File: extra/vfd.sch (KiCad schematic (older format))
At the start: 42 parts, among them P10 GU128x64E-U100, P11 gui140x16j-7002, P12 digital_in, P13 digital_out, U3 74LS125, U4 74LS125, U5 74LS125, U6 74LS125, U7 74LS125, U8 74LS245

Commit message: 3.3v is no longer connected to 5v!
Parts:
- removed R40: R?, xnorman:Resistor_Horizontal_RM10mm-xnorman, symbol R
- removed U8: 74LS245, Housings_DIP:DIP-20_W7.62mm_LongPads, symbol 74LS245
- added U8: 74LS245-xnor, Housings_DIP:DIP-20_W7.62mm_LongPads, symbol 74LS245-xnor
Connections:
- wire segments 279 -> 278
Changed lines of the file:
@@
 5v
 $Comp
-L GND #PWR018
+L GND #PWR019
 U 1 1 58578899
 P 750 650
-F 0 "#PWR018" H 750 400 50  0001 C CNN
+F 0 "#PWR019" H 750 400 50  0001 C CNN
 F 1 "GND" H 750 500 50  0000 C CNN
 F 2 "" H 750 650 50  0000 C CNN
@@
 vfdD7
 $Comp
-L GND #PWR019
+L GND #PWR020
 U 1 1 5857965E
 P 1350 7050
-F 0 "#PWR019" H 1350 6800 50  0001 C CNN
+F 0 "#PWR020" H 1350 6800 50  0001 C CNN
 F 1 "GND" H 1350 6900 50  0000 C CNN
 F 2 "" H 1350 7050 50  0000 C CNN
@@
 $EndComp
 $Comp
-L GND #PWR020
+L GND #PWR021
 U 1 1 585796B9
 P 1350 6450
-F 0 "#PWR020" H 1350 6200 50  0001 C CNN
+F 0 "#PWR021" H 1350 6200 50  0001 C CNN
 F 1 "GND" H 1350 6300 50  0000 C CNN
 F 2 "" H 1350 6450 50  0000 C CNN
@@
 $EndComp
 $Comp
-L GND #PWR021
+L GND #PWR022
 U 1 1 585796DF
 P 1350 5900
-F 0 "#PWR021" H 1350 5650 50  0001 C CNN
+F 0 "#PWR022" H 1350 5650 50  0001 C CNN
 F 1 "GND" H 1350 5750 50  0000 C CNN
 F 2 "" H 1350 5900 50  0000 C CNN
@@
 $EndComp
 $Comp
-L GND #PWR022
+L GND #PWR023
 U 1 1 5857970E
 P 1350 5250
-F 0 "#PWR022" H 1350 5000 50  0001 C CNN
+F 0 "#PWR023" H 1350 5000 50  0001 C CNN
 F 1 "GND" H 1350 5100 50  0000 C CNN
 F 2 "" H 1350 5250 50  0000 C CNN
@@
 $EndComp
 $Comp
-L GND #PWR023
+L GND #PWR024
 U 1 1 58579734
 P 1350 4750
-F 0 "#PWR023" H 1350 4500 50  0001 C CNN
+F 0 "#PWR024" H 1350 4500 50  0001 C CNN
 F 1 "GND" H 1350 4600 50  0000 C CNN
 F 2 "" H 1350 4750 50  0000 C CNN
@@
 $EndComp
 $Comp
-L GND #PWR024
+L GND #PWR025
 U 1 1 58579763
 P 1350 4150
-F 0 "#PWR024" H 1350 3900 50  0001 C CNN
+F 0 "#PWR025" H 1350 3900 50  0001 C CNN
 F 1 "GND" H 1350 4000 50  0000 C CNN
 F 2 "" H 1350 4150 50  0000 C CNN
@@
 $EndComp
 $Comp
-L GND #PWR025
+L GND #PWR026
 U 1 1 58579789
 P 1350 3600
-F 0 "#PWR025" H 1350 3350 50  0001 C CNN
+F 0 "#PWR026" H 1350 3350 50  0001 C CNN
 F 1 "GND" H 1350 3450 50  0000 C CNN
 F 2 "" H 1350 3600 50  0000 C CNN
@@
 vfdCS2
 $Comp
-L GND #PWR026
+L GND #PWR027
 U 1 1 58579E92
 P 5200 5150
-F 0 "#PWR026" H 5200 4900 50  0001 C CNN
+F 0 "#PWR027" H 5200 4900 50  0001 C CNN
 F 1 "GND" H 5200 5000 50  0000 C CNN
 F 2 "" H 5200 5150 50  0000 C CNN
@@
 $EndComp
 $Comp
-L GND #PWR027
+L GND #PWR028
 U 1 1 58579E98
 P 5200 4650
-F 0 "#PWR027" H 5200 4400 50  0001 C CNN
+F 0 "#PWR028" H 5200 4400 50  0001 C CNN
 F 1 "GND" H 5200 4500 50  0000 C CNN
 F 2 "" H 5200 4650 50  0000 C CNN
@@
 $EndComp
 $Comp
-L GND #PWR028
+L GND #PWR029
 U 1 1 58579E9E
 P 5200 4050
-F 0 "#PWR028" H 5200 3800 50  0001 C CNN
+F 0 "#PWR029" H 5200 3800 50  0001 C CNN
 F 1 "GND" H 5200 3900 50  0000 C CNN
 F 2 "" H 5200 4050 50  0000 C CNN
@@
 $EndComp
 $Comp
-L GND #PWR029
+L GND #PWR030
 U 1 1 58579EA4
 P 5200 3500
-F 0 "#PWR029" H 5200 3250 50  0001 C CNN
+F 0 "#PWR030" H 5200 3250 50  0001 C CNN
 F 1 "GND" H 5200 3350 50  0000 C CNN
 F 2 "" H 5200 3500 50  0000 C CNN
@@
 moddigout4
 $Comp
-L GND #PWR030
+L GND #PWR031
 U 1 1 5857A461
 P 5200 7450
-F 0 "#PWR030" H 5200 7200 50  0001 C CNN
+F 0 "#PWR031" H 5200 7200 50  0001 C CNN
 F 1 "GND" H 5200 7300 50  0000 C CNN
 F 2 "" H 5200 7450 50  0000 C CNN
@@
 $EndComp
 $Comp
-L GND #PWR031
+L GND #PWR032
 U 1 1 5857A467
 P 5200 6950
-F 0 "#PWR031" H 5200 6700 50  0001 C CNN
+F 0 "#PWR032" H 5200 6700 50  0001 C CNN
 F 1 "GND" H 5200 6800 50  0000 C CNN
 F 2 "" H 5200 6950 50  0000 C CNN
@@
 $EndComp
 $Comp
-L GND #PWR032
+L GND #PWR033
 U 1 1 5857A46D
 P 5200 6350
-F 0 "#PWR032" H 5200 6100 50  0001 C CNN
+F 0 "#PWR033" H 5200 6100 50  0001 C CNN
 F 1 "GND" H 5200 6200 50  0000 C CNN
 F 2 "" H 5200 6350 50  0000 C CNN
@@
 $EndComp
 $Comp
-L GND #PWR033
+L GND #PWR034
 U 1 1 5857A473
 P 5200 5800
-F 0 "#PWR033" H 5200 5550 50  0001 C CNN
+F 0 "#PWR034" H 5200 5550 50  0001 C CNN
 F 1 "GND" H 5200 5650 50  0000 C CNN
 F 2 "" H 5200 5800 50  0000 C CNN
@@
 3.3v
 $Comp
-L GND #PWR034
+L GND #PWR035
 U 1 1 5857B8FE
 P 9650 2550
-F 0 "#PWR034" H 9650 2300 50  0001 C CNN
+F 0 "#PWR035" H 9650 2300 50  0001 C CNN
 F 1 "GND" H 9650 2400 50  0000 C CNN
 F 2 "" H 9650 2550 50  0000 C CNN
@@
 	5200 7450 5600 7450
 Wire Wire Line
+	8650 1800 8950 1800
+Wire Wire Line
 	9650 2350 9650 2550
 Wire Wire Line
@@
 $EndComp
 $Comp
-L GND #PWR035
+L GND #PWR036
 U 1 1 586B1181
 P -700 950
-F 0 "#PWR035" H -700 700 50  0001 C CNN
+F 0 "#PWR036" H -700 700 50  0001 C CNN
 F 1 "GND" H -700 800 50  0000 C CNN
 F 2 "" H -700 950 50  0000 C CNN
@@
 Wire Wire Line
 	8650 1700 8950 1700
-Wire Wire Line
-	8650 1800 8950 1800
 Text GLabel 10550 1700 2    60   Output ~ 0
 beladigin5
@@
 vfdE
 $Comp
-L GND #PWR036
+L GND #PWR037
 U 1 1 586B61FC
 P 8800 6450
-F 0 "#PWR036" H 8800 6200 50  0001 C CNN
+F 0 "#PWR037" H 8800 6200 50  0001 C CNN
 F 1 "GND" H 8800 6300 50  0000 C CNN
 F 2 "" H 8800 6450 50  0000 C CNN
@@
 $EndComp
 $Comp
-L GND #PWR037
+L GND #PWR038
 U 1 1 586B6202
 P 8800 5950
-F 0 "#PWR037" H 8800 5700 50  0001 C CNN
+F 0 "#PWR038" H 8800 5700 50  0001 C CNN
 F 1 "GND" H 8800 5800 50  0000 C CNN
 F 2 "" H 8800 5950 50  0000 C CNN
@@
 $EndComp
 $Comp
-L GND #PWR038
+L GND #PWR039
 U 1 1 586B6208
 P 8800 5350
-F 0 "#PWR038" H 8800 5100 50  0001 C CNN
+F 0 "#PWR039" H 8800 5100 50  0001 C CNN
 F 1 "GND" H 8800 5200 50  0000 C CNN
 F 2 "" H 8800 5350 50  0000 C CNN
@@
 $EndComp
 $Comp
-L GND #PWR039
+L GND #PWR040
 U 1 1 586B620E
 P 8800 4800
-F 0 "#PWR039" H 8800 4550 50  0001 C CNN
+F 0 "#PWR040" H 8800 4550 50  0001 C CNN
 F 1 "GND" H 8800 4650 50  0000 C CNN
 F 2 "" H 8800 4800 50  0000 C CNN
@@
 	3250 1750 4150 1750
 $Comp
-L GND #PWR040
+L GND #PWR041
 U 1 1 586B38A8
 P 3250 2150
-F 0 "#PWR040" H 3250 1900 50  0001 C CNN
+F 0 "#PWR041" H 3250 1900 50  0001 C CNN
 F 1 "GND" H 3250 2000 50  0000 C CNN
 F 2 "" H 3250 2150 50  0000 C CNN
@@
 	6700 2050 6850 2050
 $Comp
-L GND #PWR041
+L GND #PWR042
 U 1 1 586B6695
 P 6600 2200
-F 0 "#PWR041" H 6600 1950 50  0001 C CNN
+F 0 "#PWR042" H 6600 1950 50  0001 C CNN
 F 1 "GND" H 6600 2050 50  0000 C CNN
 F 2 "" H 6600 2200 50  0000 C CNN
@@
 Connection ~ 5400 1250
 $Comp
-L GND #PWR042
+L GND #PWR043
 U 1 1 586B8342
 P 5400 2350
-F 0 "#PWR042" H 5400 2100 50  0001 C CNN
+F 0 "#PWR043" H 5400 2100 50  0001 C CNN
 F 1 "GND" H 5400 2200 50  0000 C CNN
 F 2 "" H 5400 2350 50  0000 C CNN
@@
 digital input protection, needed if we're using level shifter???
 $Comp
-L GND #PWR043
+L GND #PWR044
 U 1 1 586B5219
 P 4350 2550
-F 0 "#PWR043" H 4350 2300 50  0001 C CNN
+F 0 "#PWR044" H 4350 2300 50  0001 C CNN
 F 1 "GND" H 4350 2400 50  0000 C CNN
 F 2 "" H 4350 2550 50  0000 C CNN
@@
 NoConn ~ 1250 750
 NoConn ~ -450 1250
-NoConn ~ 10350 1900
-$Comp
-L R R40
-U 1 1 586D568E
-P 8150 2100
-F 0 "R40" V 8230 2100 50  0000 C CNN
-F 1 "R?" V 8150 2100 50  0000 C CNN
-F 2 "xnorman:Resistor_Horizontal_RM10mm-xnorman" V 8080 2100 50  0001 C CNN
-F 3 "" H 8150 2100 50  0000 C CNN
-	1    8150 2100
-	-1   0    0    1
-$EndComp
 Wire Wire Line
 	8950 1900 8150 1900
 Wire Wire Line
-	8150 1900 8150 1950
-Wire Wire Line
-	8150 2250 8150 2450
+	8150 1900 8150 2450
 Wire Wire Line
 	8850 2300 8850 2450
@@
 Wire Wire Line
 	9650 1050 9650 1250
-$Comp
-L 74LS245 U8
-U 1 1 586E215C
+NoConn ~ 10350 1900
+$Comp
+L 74LS245-xnor U8
+U 1 1 586F0C65
 P 9650 1800
 F 0 "U8" H 9750 2375 50  0000 L BNN
-F 1 "74LS245" H 9700 1225 50  0000 L TNN
+F 1 "74LS245-xnor" H 9700 1225 50  0000 L TNN
 F 2 "Housings_DIP:DIP-20_W7.62mm_LongPads" H 9650 1800 50  0001 C CNN
 F 3 "" H 9650 1800 50  0000 C CNN

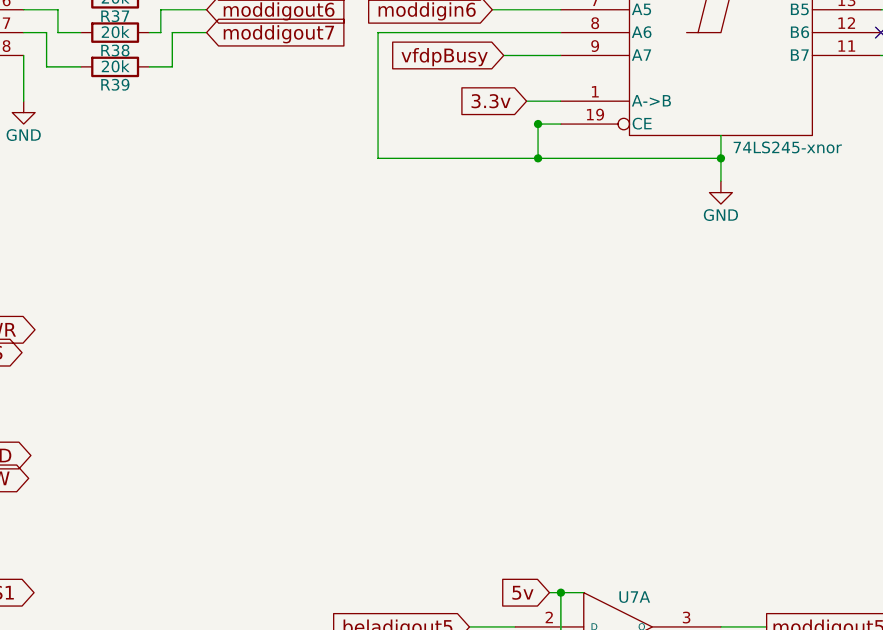
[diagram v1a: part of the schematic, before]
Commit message: added decoupling caps, power expand, more layout
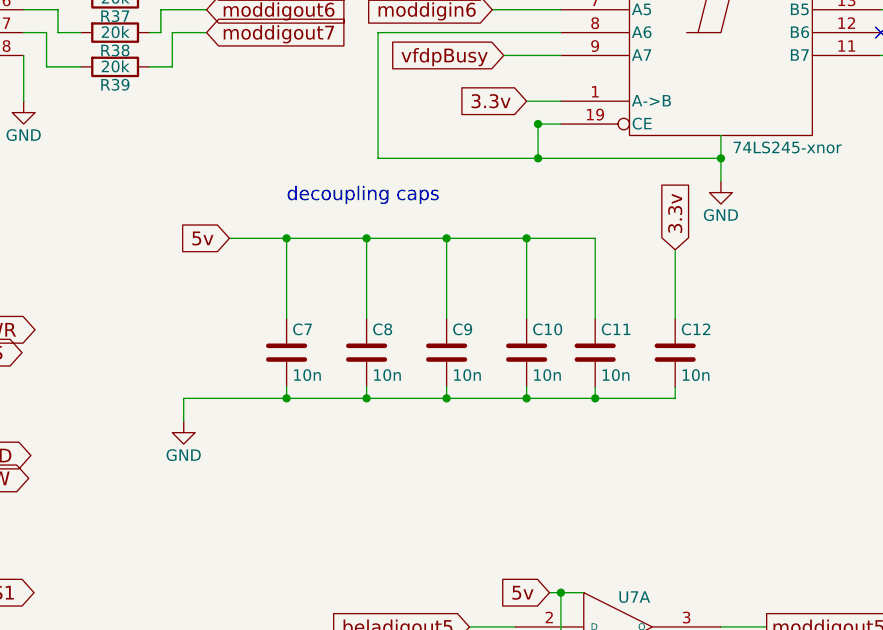
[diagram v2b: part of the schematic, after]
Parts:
- added C10, C11, C12, C7, C8, C9: 10n, Capacitors_ThroughHole:C_Rect_L4_W2.5_P2.5, symbol C
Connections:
- net 3.3v: now also C12.1
- net GND: now also C10.2, C11.2, C12.2, C7.2, C8.2, C9.2
- net VCC: now also C10.1, C11.1, C7.1, C8.1, C9.1
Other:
- note added: "decoupling caps"
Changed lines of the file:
@@
 5v
 $Comp
-L GND #PWR019
+L GND #PWR17
 U 1 1 58578899
 P 750 650
-F 0 "#PWR019" H 750 400 50  0001 C CNN
+F 0 "#PWR17" H 750 400 50  0001 C CNN
 F 1 "GND" H 750 500 50  0000 C CNN
 F 2 "" H 750 650 50  0000 C CNN
@@
 vfdD7
 $Comp
-L GND #PWR020
+L GND #PWR24
 U 1 1 5857965E
 P 1350 7050
-F 0 "#PWR020" H 1350 6800 50  0001 C CNN
+F 0 "#PWR24" H 1350 6800 50  0001 C CNN
 F 1 "GND" H 1350 6900 50  0000 C CNN
 F 2 "" H 1350 7050 50  0000 C CNN
@@
 $EndComp
 $Comp
-L GND #PWR021
+L GND #PWR23
 U 1 1 585796B9
 P 1350 6450
-F 0 "#PWR021" H 1350 6200 50  0001 C CNN
+F 0 "#PWR23" H 1350 6200 50  0001 C CNN
 F 1 "GND" H 1350 6300 50  0000 C CNN
 F 2 "" H 1350 6450 50  0000 C CNN
@@
 $EndComp
 $Comp
-L GND #PWR022
+L GND #PWR22
 U 1 1 585796DF
 P 1350 5900
-F 0 "#PWR022" H 1350 5650 50  0001 C CNN
+F 0 "#PWR22" H 1350 5650 50  0001 C CNN
 F 1 "GND" H 1350 5750 50  0000 C CNN
 F 2 "" H 1350 5900 50  0000 C CNN
@@
 $EndComp
 $Comp
-L GND #PWR023
+L GND #PWR21
 U 1 1 5857970E
 P 1350 5250
-F 0 "#PWR023" H 1350 5000 50  0001 C CNN
+F 0 "#PWR21" H 1350 5000 50  0001 C CNN
 F 1 "GND" H 1350 5100 50  0000 C CNN
 F 2 "" H 1350 5250 50  0000 C CNN
@@
 $EndComp
 $Comp
-L GND #PWR024
+L GND #PWR20
 U 1 1 58579734
 P 1350 4750
-F 0 "#PWR024" H 1350 4500 50  0001 C CNN
+F 0 "#PWR20" H 1350 4500 50  0001 C CNN
 F 1 "GND" H 1350 4600 50  0000 C CNN
 F 2 "" H 1350 4750 50  0000 C CNN
@@
 $EndComp
 $Comp
-L GND #PWR025
+L GND #PWR19
 U 1 1 58579763
 P 1350 4150
-F 0 "#PWR025" H 1350 3900 50  0001 C CNN
+F 0 "#PWR19" H 1350 3900 50  0001 C CNN
 F 1 "GND" H 1350 4000 50  0000 C CNN
 F 2 "" H 1350 4150 50  0000 C CNN
@@
 $EndComp
 $Comp
-L GND #PWR026
+L GND #PWR18
 U 1 1 58579789
 P 1350 3600
-F 0 "#PWR026" H 1350 3350 50  0001 C CNN
+F 0 "#PWR18" H 1350 3350 50  0001 C CNN
 F 1 "GND" H 1350 3450 50  0000 C CNN
 F 2 "" H 1350 3600 50  0000 C CNN
@@
 vfdCS2
 $Comp
-L GND #PWR027
+L GND #PWR30
 U 1 1 58579E92
 P 5200 5150
-F 0 "#PWR027" H 5200 4900 50  0001 C CNN
+F 0 "#PWR30" H 5200 4900 50  0001 C CNN
 F 1 "GND" H 5200 5000 50  0000 C CNN
 F 2 "" H 5200 5150 50  0000 C CNN
@@
 $EndComp
 $Comp
-L GND #PWR028
+L GND #PWR29
 U 1 1 58579E98
 P 5200 4650
-F 0 "#PWR028" H 5200 4400 50  0001 C CNN
+F 0 "#PWR29" H 5200 4400 50  0001 C CNN
 F 1 "GND" H 5200 4500 50  0000 C CNN
 F 2 "" H 5200 4650 50  0000 C CNN
@@
 $EndComp
 $Comp
-L GND #PWR029
+L GND #PWR28
 U 1 1 58579E9E
 P 5200 4050
-F 0 "#PWR029" H 5200 3800 50  0001 C CNN
+F 0 "#PWR28" H 5200 3800 50  0001 C CNN
 F 1 "GND" H 5200 3900 50  0000 C CNN
 F 2 "" H 5200 4050 50  0000 C CNN
@@
 $EndComp
 $Comp
-L GND #PWR030
+L GND #PWR27
 U 1 1 58579EA4
 P 5200 3500
-F 0 "#PWR030" H 5200 3250 50  0001 C CNN
+F 0 "#PWR27" H 5200 3250 50  0001 C CNN
 F 1 "GND" H 5200 3350 50  0000 C CNN
 F 2 "" H 5200 3500 50  0000 C CNN
@@
 moddigout4
 $Comp
-L GND #PWR031
+L GND #PWR34
 U 1 1 5857A461
 P 5200 7450
-F 0 "#PWR031" H 5200 7200 50  0001 C CNN
+F 0 "#PWR34" H 5200 7200 50  0001 C CNN
 F 1 "GND" H 5200 7300 50  0000 C CNN
 F 2 "" H 5200 7450 50  0000 C CNN
@@
 $EndComp
 $Comp
-L GND #PWR032
+L GND #PWR33
 U 1 1 5857A467
 P 5200 6950
-F 0 "#PWR032" H 5200 6700 50  0001 C CNN
+F 0 "#PWR33" H 5200 6700 50  0001 C CNN
 F 1 "GND" H 5200 6800 50  0000 C CNN
 F 2 "" H 5200 6950 50  0000 C CNN
@@
 $EndComp
 $Comp
-L GND #PWR033
+L GND #PWR32
 U 1 1 5857A46D
 P 5200 6350
-F 0 "#PWR033" H 5200 6100 50  0001 C CNN
+F 0 "#PWR32" H 5200 6100 50  0001 C CNN
 F 1 "GND" H 5200 6200 50  0000 C CNN
 F 2 "" H 5200 6350 50  0000 C CNN
@@
 $EndComp
 $Comp
-L GND #PWR034
+L GND #PWR31
 U 1 1 5857A473
 P 5200 5800
-F 0 "#PWR034" H 5200 5550 50  0001 C CNN
+F 0 "#PWR31" H 5200 5550 50  0001 C CNN
 F 1 "GND" H 5200 5650 50  0000 C CNN
 F 2 "" H 5200 5800 50  0000 C CNN
@@
 3.3v
 $Comp
-L GND #PWR035
+L GND #PWR42
 U 1 1 5857B8FE
 P 9650 2550
-F 0 "#PWR035" H 9650 2300 50  0001 C CNN
+F 0 "#PWR42" H 9650 2300 50  0001 C CNN
 F 1 "GND" H 9650 2400 50  0000 C CNN
 F 2 "" H 9650 2550 50  0000 C CNN
@@
 $EndComp
 $Comp
-L GND #PWR036
+L GND #PWR16
 U 1 1 586B1181
 P -700 950
-F 0 "#PWR036" H -700 700 50  0001 C CNN
+F 0 "#PWR16" H -700 700 50  0001 C CNN
 F 1 "GND" H -700 800 50  0000 C CNN
 F 2 "" H -700 950 50  0000 C CNN
@@
 vfdE
 $Comp
-L GND #PWR037
+L GND #PWR41
 U 1 1 586B61FC
 P 8800 6450
-F 0 "#PWR037" H 8800 6200 50  0001 C CNN
+F 0 "#PWR41" H 8800 6200 50  0001 C CNN
 F 1 "GND" H 8800 6300 50  0000 C CNN
 F 2 "" H 8800 6450 50  0000 C CNN
@@
 $EndComp
 $Comp
-L GND #PWR038
+L GND #PWR40
 U 1 1 586B6202
 P 8800 5950
-F 0 "#PWR038" H 8800 5700 50  0001 C CNN
+F 0 "#PWR40" H 8800 5700 50  0001 C CNN
 F 1 "GND" H 8800 5800 50  0000 C CNN
 F 2 "" H 8800 5950 50  0000 C CNN
@@
 $EndComp
 $Comp
-L GND #PWR039
+L GND #PWR39
 U 1 1 586B6208
 P 8800 5350
-F 0 "#PWR039" H 8800 5100 50  0001 C CNN
+F 0 "#PWR39" H 8800 5100 50  0001 C CNN
 F 1 "GND" H 8800 5200 50  0000 C CNN
 F 2 "" H 8800 5350 50  0000 C CNN
@@
 $EndComp
 $Comp
-L GND #PWR040
+L GND #PWR38
 U 1 1 586B620E
 P 8800 4800
-F 0 "#PWR040" H 8800 4550 50  0001 C CNN
+F 0 "#PWR38" H 8800 4550 50  0001 C CNN
 F 1 "GND" H 8800 4650 50  0000 C CNN
 F 2 "" H 8800 4800 50  0000 C CNN
@@
 	3250 1750 4150 1750
 $Comp
-L GND #PWR041
+L GND #PWR25
 U 1 1 586B38A8
 P 3250 2150
-F 0 "#PWR041" H 3250 1900 50  0001 C CNN
+F 0 "#PWR25" H 3250 1900 50  0001 C CNN
 F 1 "GND" H 3250 2000 50  0000 C CNN
 F 2 "" H 3250 2150 50  0000 C CNN
@@
 	6700 2050 6850 2050
 $Comp
-L GND #PWR042
+L GND #PWR36
 U 1 1 586B6695
 P 6600 2200
-F 0 "#PWR042" H 6600 1950 50  0001 C CNN
+F 0 "#PWR36" H 6600 1950 50  0001 C CNN
 F 1 "GND" H 6600 2050 50  0000 C CNN
 F 2 "" H 6600 2200 50  0000 C CNN
@@
 Connection ~ 5400 1250
 $Comp
-L GND #PWR043
+L GND #PWR35
 U 1 1 586B8342
 P 5400 2350
-F 0 "#PWR043" H 5400 2100 50  0001 C CNN
+F 0 "#PWR35" H 5400 2100 50  0001 C CNN
 F 1 "GND" H 5400 2200 50  0000 C CNN
 F 2 "" H 5400 2350 50  0000 C CNN
@@
 digital input protection, needed if we're using level shifter???
 $Comp
-L GND #PWR044
+L GND #PWR26
 U 1 1 586B5219
 P 4350 2550
-F 0 "#PWR044" H 4350 2300 50  0001 C CNN
+F 0 "#PWR26" H 4350 2300 50  0001 C CNN
 F 1 "GND" H 4350 2400 50  0000 C CNN
 F 2 "" H 4350 2550 50  0000 C CNN
@@
 	1    0    0    -1
 $EndComp
+$Comp
+L C C7
+U 1 1 5871C2E4
+P 7750 3300
+F 0 "C7" H 7775 3400 50  0000 L CNN
+F 1 "10n" H 7775 3200 50  0000 L CNN
+F 2 "Capacitors_ThroughHole:C_Rect_L4_W2.5_P2.5" H 7788 3150 50  0001 C CNN
+F 3 "" H 7750 3300 50  0000 C CNN
+	1    7750 3300
+	1    0    0    -1
+$EndComp
+$Comp
+L C C8
+U 1 1 5871C2F2
+P 8100 3300
+F 0 "C8" H 8125 3400 50  0000 L CNN
+F 1 "10n" H 8125 3200 50  0000 L CNN
+F 2 "Capacitors_ThroughHole:C_Rect_L4_W2.5_P2.5" H 8138 3150 50  0001 C CNN
+F 3 "" H 8100 3300 50  0000 C CNN
+	1    8100 3300
+	1    0    0    -1
+$EndComp
+$Comp
+L C C9
+U 1 1 5871C300
+P 8450 3300
+F 0 "C9" H 8475 3400 50  0000 L CNN
+F 1 "10n" H 8475 3200 50  0000 L CNN
+F 2 "Capacitors_ThroughHole:C_Rect_L4_W2.5_P2.5" H 8488 3150 50  0001 C CNN
+F 3 "" H 8450 3300 50  0000 C CNN
+	1    8450 3300
+	1    0    0    -1
+$EndComp
+Text GLabel 7500 2800 0    60   Input ~ 0
+5v
+$Comp
+L GND #PWR37
+U 1 1 5871C310
+P 7300 3600
+F 0 "#PWR37" H 7300 3350 50  0001 C CNN
+F 1 "GND" H 7300 3450 50  0000 C CNN
+F 2 "" H 7300 3600 50  0000 C CNN
+F 3 "" H 7300 3600 50  0000 C CNN
+	1    7300 3600
+	1    0    0    -1
+$EndComp
+Text Notes 7750 2650 0    60   ~ 0
+decoupling caps
+Wire Wire Line
+	7750 2800 7750 3150
+Wire Wire Line
+	8100 2800 8100 3150
+Wire Wire Line
+	8450 2800 8450 3150
+Wire Wire Line
+	7300 3600 7300 3500
+Wire Wire Line
+	7300 3500 9450 3500
+Wire Wire Line
+	7500 2800 9100 2800
+Connection ~ 7750 2800
+Connection ~ 8100 2800
+Wire Wire Line
+	7750 3450 7750 3500
+Connection ~ 7750 3500
+Wire Wire Line
+	8100 3450 8100 3500
+Connection ~ 8100 3500
+Wire Wire Line
+	8450 3500 8450 3450
+$Comp
+L C C10
+U 1 1 5871D0FD
+P 8800 3300
+F 0 "C10" H 8825 3400 50  0000 L CNN
+F 1 "10n" H 8825 3200 50  0000 L CNN
+F 2 "Capacitors_ThroughHole:C_Rect_L4_W2.5_P2.5" H 8838 3150 50  0001 C CNN
+F 3 "" H 8800 3300 50  0000 C CNN
+	1    8800 3300
+	1    0    0    -1
+$EndComp
+$Comp
+L C C11
+U 1 1 5871D1CB
+P 9100 3300
+F 0 "C11" H 9125 3400 50  0000 L CNN
+F 1 "10n" H 9125 3200 50  0000 L CNN
+F 2 "Capacitors_ThroughHole:C_Rect_L4_W2.5_P2.5" H 9138 3150 50  0001 C CNN
+F 3 "" H 9100 3300 50  0000 C CNN
+	1    9100 3300
+	1    0    0    -1
+$EndComp
+$Comp
+L C C12
+U 1 1 5871D29E
+P 9450 3300
+F 0 "C12" H 9475 3400 50  0000 L CNN
+F 1 "10n" H 9475 3200 50  0000 L CNN
+F 2 "Capacitors_ThroughHole:C_Rect_L4_W2.5_P2.5" H 9488 3150 50  0001 C CNN
+F 3 "" H 9450 3300 50  0000 C CNN
+	1    9450 3300
+	1    0    0    -1
+$EndComp
+Wire Wire Line
+	8800 2800 8800 3150
+Connection ~ 8450 2800
+Wire Wire Line
+	9100 2800 9100 3150
+Connection ~ 8800 2800
+Wire Wire Line
+	9100 3500 9100 3450
+Connection ~ 8450 3500
+Wire Wire Line
+	8800 3450 8800 3500
+Connection ~ 8800 3500
+Wire Wire Line
+	9450 3500 9450 3450
+Connection ~ 9100 3500
+Text GLabel 9450 2850 1    60   Input ~ 0
+3.3v
+Wire Wire Line
+	9450 2850 9450 3150
 $EndSCHEMATC
